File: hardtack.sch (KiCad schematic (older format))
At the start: 2 parts, among them U1 Teensy-LC

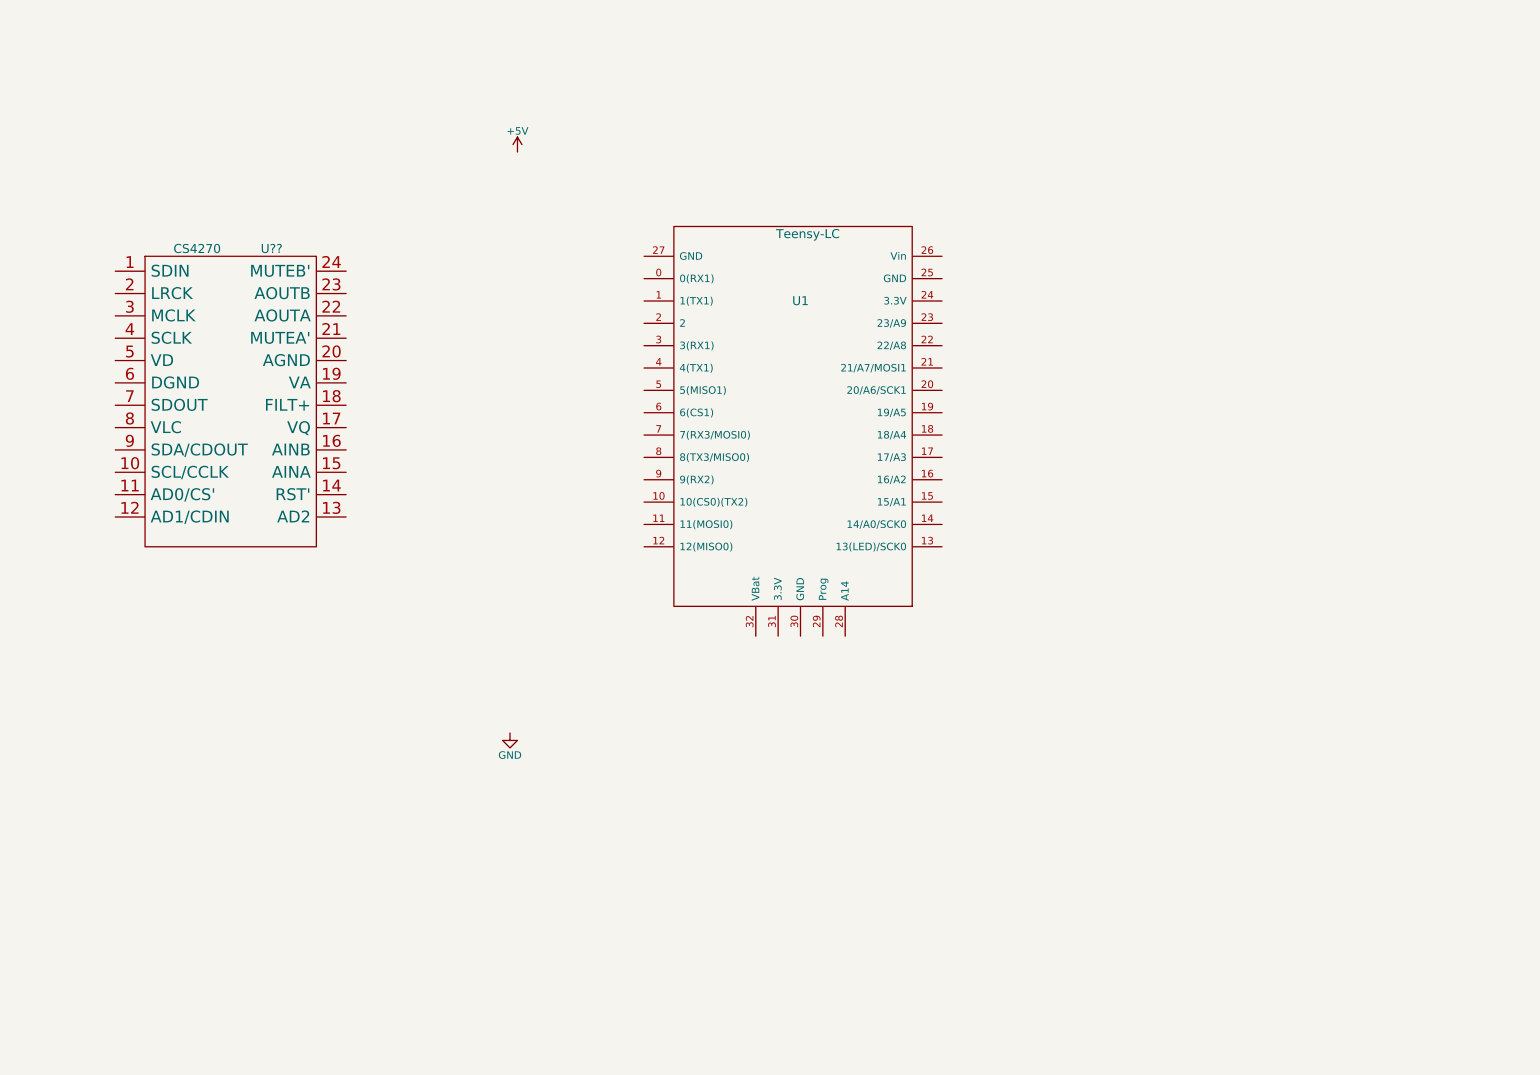
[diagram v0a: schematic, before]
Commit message: More spi bus work and add adafruit display
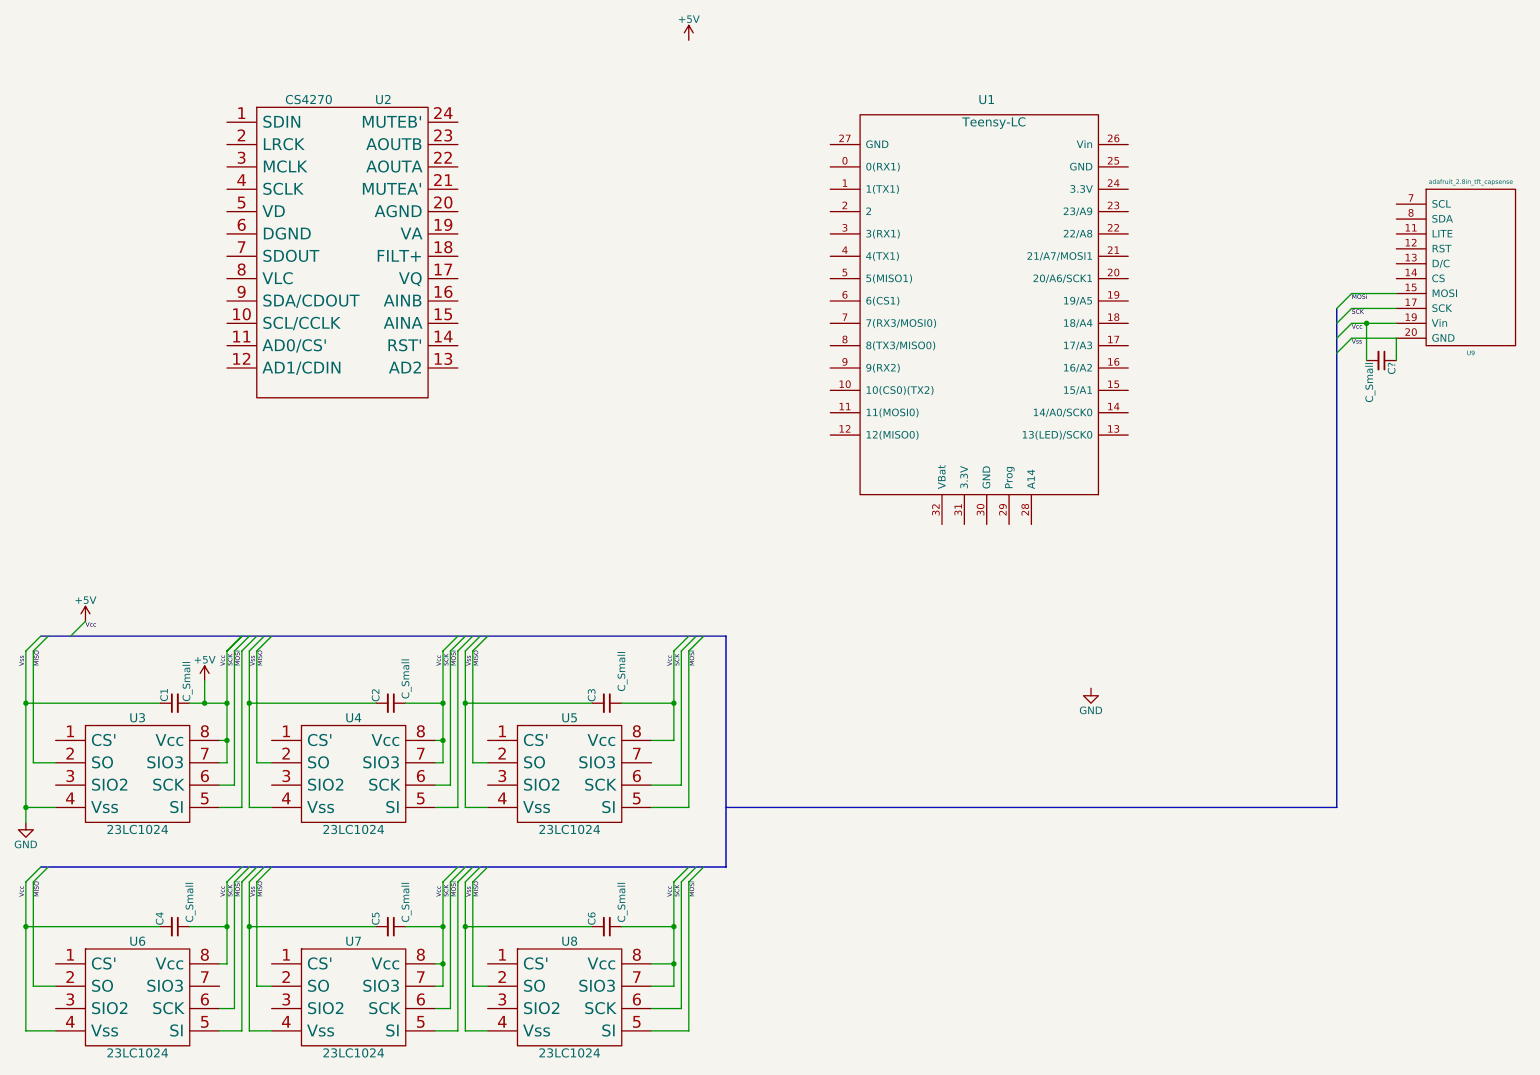
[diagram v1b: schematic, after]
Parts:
- added C1, C2, C3, C4, C5, C6, C?: C_Small, symbol C_Small
- added U3, U4, U5, U6, U7, U8: 23LC1024, symbol 23LC1024
- added U9: adafruit_2.8in_tft_capsense, symbol adafruit_2.8in_tft_capsense
- gave numbers to parts that had none: 1
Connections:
- net +5V: now also C1.2, C2.1, C3.1, C4.1, C4.2, C5.1, C6.1, U3.7 (SIO3), U3.8 (Vcc), U4.7 (SIO3), U4.8 (Vcc), U5.8 (Vcc), U6.4 (Vss), U6.8 (Vcc), U7.7 (SIO3), U7.8 (Vcc), U8.7 (SIO3), U8.8 (Vcc)
- net GND: now also C1.1, U3.4 (Vss), U4.2 (SO), U5.2 (SO), U7.2 (SO), U8.2 (SO)
- new net: C2.2, U4.4 (Vss)
- new net: C3.2, U5.4 (Vss)
- new net: C5.2, U7.4 (Vss)
- new net: C6.2, U8.4 (Vss)
- new net: C?.2, U9.19 (Vin)
- new net: C?.1, U9.20 (GND)
- new net MOSI: U3.5 (SI), U4.5 (SI), U6.5 (SI), U7.5 (SI)
- new net SCK: U3.6 (SCK), U4.6 (SCK), U5.6 (SCK), U6.6 (SCK), U7.6 (SCK), U8.6 (SCK)
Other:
- moved on the sheet: U1, U2

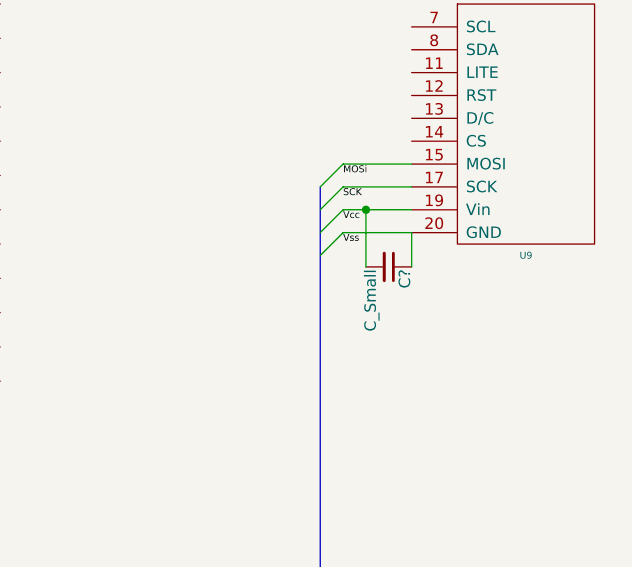
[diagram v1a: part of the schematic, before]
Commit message: just a cap label
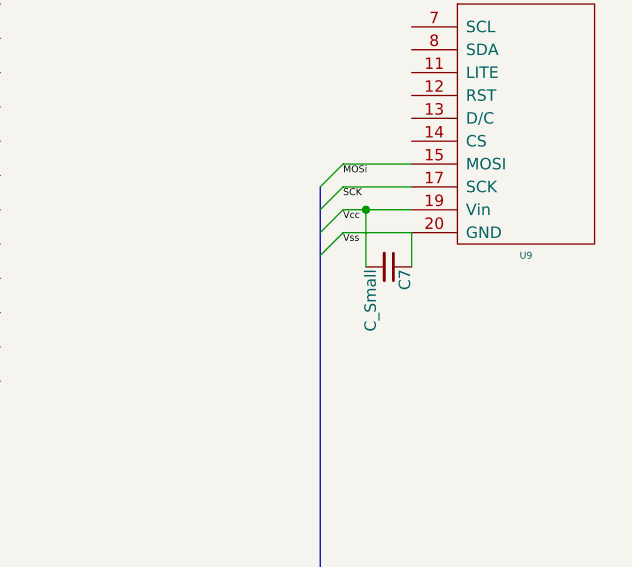
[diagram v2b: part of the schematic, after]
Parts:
- gave numbers to parts that had none: 1
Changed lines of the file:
@@
 $EndComp
 $Comp
-L +5V #PWR?
+L +5V #PWR01
 U 1 1 55B479B7
 P 5200 750
-F 0 "#PWR?" H 5200 600 50  0001 C CNN
+F 0 "#PWR01" H 5200 600 50  0001 C CNN
 F 1 "+5V" H 5200 890 50  0000 C CNN
 F 2 "" H 5200 750 60  0000 C CNN
@@
 $EndComp
 $Comp
-L GND #PWR?
+L GND #PWR02
 U 1 1 55B479CC
 P 7900 5100
-F 0 "#PWR?" H 7900 4850 50  0001 C CNN
+F 0 "#PWR02" H 7900 4850 50  0001 C CNN
 F 1 "GND" H 7900 4950 50  0000 C CNN
 F 2 "" H 7900 5100 60  0000 C CNN
@@
 Vcc
 $Comp
-L +5V #PWR?
+L +5V #PWR03
 U 1 1 55B595AC
 P 1950 5050
-F 0 "#PWR?" H 1950 4900 50  0001 C CNN
+F 0 "#PWR03" H 1950 4900 50  0001 C CNN
 F 1 "+5V" H 1950 5190 50  0000 C CNN
 F 2 "" H 1950 5050 60  0000 C CNN
@@
 $EndComp
 $Comp
-L GND #PWR?
+L GND #PWR04
 U 1 1 55B595DC
 P 750 6000
-F 0 "#PWR?" H 750 5750 50  0001 C CNN
+F 0 "#PWR04" H 750 5750 50  0001 C CNN
 F 1 "GND" H 750 5850 50  0000 C CNN
 F 2 "" H 750 6000 60  0000 C CNN
@@
 SCK
 $Comp
-L +5V #PWR?
+L +5V #PWR05
 U 1 1 55C05CDA
 P 1150 4650
-F 0 "#PWR?" H 1150 4500 50  0001 C CNN
+F 0 "#PWR05" H 1150 4500 50  0001 C CNN
 F 1 "+5V" H 1150 4790 50  0000 C CNN
 F 2 "" H 1150 4650 60  0000 C CNN
@@
 Vss
 $Comp
-L C_Small C?
+L C_Small C7
 U 1 1 55C09124
 P 9850 2900
-F 0 "C?" H 9860 2970 50  0000 L CNN
+F 0 "C7" H 9860 2970 50  0000 L CNN
 F 1 "C_Small" H 9860 2820 50  0000 L CNN
 F 2 "" H 9850 2900 60  0000 C CNN
